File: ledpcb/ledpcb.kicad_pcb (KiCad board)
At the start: 2 copper layers, 12 parts, among them J1 USB_C_Receptacle_USB2.0, J2 Conn_01x04_Male, Q1 ME2306A, Q2 ME2306A, Q3 ME2306A, SW1 SW_Push, U1 SPX3819M5-L-3-3_TR, U2 ESP32-WROOM-32

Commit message: version
Signed-off-by: 3nt3 <gott@3nt3.de>
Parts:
- removed R4: 5.1k, Resistor_SMD:R_1206_3216Metric_Pad1.30x1.75mm_HandSolder
- added J3: Barrel_Jack, Library:DEALON DC-S050-200, F.Cu at (108.0, 109.6)
- added J4: Conn_01x04_Male, Connector_PinHeader_2.00mm:PinHeader_1x04_P2.00mm_Horizontal, F.Cu at (146.8, 100.6)
- added U3: TMP100, Package_TO_SOT_SMD:SOT-23-6, F.Cu at (106.9, 98.0)
- J1: value USB_C_Receptacle_USB2.0 -> Conn_01x02_Female; footprint Connector_USB:USB_C_Receptacle_GCT_USB4085 -> Connector_PinHeader_1.27mm:PinHeader_1x02_P1.27mm_Vertical
- J2: value Conn_01x04_Male -> Conn_01x04_Female
- R1: value 1M -> 5.1k
- R2, R3: value 5.1k -> 5K1; footprint Resistor_SMD:R_1206_3216Metric_Pad1.30x1.75mm_HandSolder -> Resistor_SMD:R_0603_1608Metric_Pad0.98x0.95mm_HandSolder
- SW1: footprint Button_Switch_SMD:SW_Push_1P1T_NO_CK_KSC6xxJ -> easyeda2kicad:KEY-SMD_4P-L6.2-W6.5-P4.50-LS8.0_SKHMXX
- moved R2 51.8 mm to (103.5, 96.8), turned to 0 degrees
- moved R1 40.3 mm to (115.1, 97.6), turned to 90 degrees
- moved J2 31.7 mm to (146.8, 86.0), turned to 0 degrees
- moved Q2 25.7 mm to (140.5, 107.6), turned to 180 degrees
- moved Q1 23.9 mm to (140.5, 101.0), turned to 180 degrees
- moved Q3 22.0 mm to (140.5, 104.3), turned to 180 degrees
- moved SW1 21.5 mm to (107.1, 88.6), turned to -90 degrees
- moved U1 15.2 mm to (142.8, 97.2), turned to -90 degrees
- moved J1 15.2 mm to (146.8, 95.8), turned to 0 degrees
- moved R3 15.0 mm to (103.4, 98.4)
- moved U2 11.5 mm to (126.7, 99.2)
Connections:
- J2 pad 1: GND -> +3V3
- J2 pad 2: Net-(J2-Pad2) -> GND
- J2 pad 3: Net-(J2-Pad3) -> TX
- J2 pad 4: Net-(J2-Pad4) -> GND
- Q1 pad 3: Net-(J2-Pad4) -> Net-(J4-Pad4)
- Q2 pad 3: Net-(J2-Pad3) -> Net-(J4-Pad3)
- Q3 pad 3: Net-(J2-Pad2) -> Net-(J4-Pad2)
- R1 pad 1: Net-(J1-PadS1) -> EN
- R1 pad 2: GND -> +3V3
- R2 pad 1: Net-(J1-PadB5) -> +3V3
- R2 pad 2: GND -> SCL
- R3 pad 1: EN -> +3V3
- R3 pad 2: +3V3 -> SDA
- U2 pad 23: RED_CHANNEL -> unconnected-(U2-Pad23)
- U2 pad 25: unconnected-(U2-Pad25) -> IO0/BOOT
- U2 pad 29: unconnected-(U2-Pad29) -> RED_CHANNEL
- U2 pad 33: unconnected-(U2-Pad33) -> SDA
- U2 pad 34: unconnected-(U2-Pad34) -> GND
- U2 pad 35: unconnected-(U2-Pad35) -> TX
- U2 pad 36: unconnected-(U2-Pad36) -> SCL
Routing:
- net +3V3: track 0.00 -> 62.8 mm, vias 0 -> 4
- net +5V: track 20.2 -> 63.7 mm
- net SCL: track 0.00 -> 41.1 mm, vias 0 -> 4
- net SDA: track 0.00 -> 35.4 mm, vias 0 -> 2
- net GND: track 0.00 -> 34.1 mm, vias 0 -> 6
- net EN: track 0.00 -> 20.0 mm
- net IO0/BOOT: track 0.00 -> 18.7 mm, vias 0 -> 2
- net Net-(J1-PadB5): track 14.7 -> 0.00 mm, vias 1 -> 0
- net TX: track 0.00 -> 13.5 mm
- net Net-(J4-Pad4): track 0.00 -> 12.2 mm, vias 0 -> 2
- net Net-(J1-PadS1): track 9.67 -> 0.00 mm
- net Net-(J4-Pad3): track 0.00 -> 6.35 mm
- net unconnected-(J1-PadA5): track 5.87 -> 0.00 mm
- net Net-(J4-Pad2): track 0.00 -> 5.79 mm
- net RED_CHANNEL: track 0.00 -> 5.12 mm
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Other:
- board outline added: 49 x 35.8 mm
- board text added: "LED Controller v1"
- board text added: "© 3nt3 2022"

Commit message: progress
Signed-off-by: 3nt3 <gott@3nt3.de>
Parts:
- added REF**: MountingHole_3.2mm_M3, MountingHole:MountingHole_3.2mm_M3, F.Cu at (106.4, 78.2)
- added REF**: MountingHole_3.2mm_M3, MountingHole:MountingHole_3.2mm_M3, F.Cu at (144.9, 122.5)
- added REF**: MountingHole_3.2mm_M3, MountingHole:MountingHole_3.2mm_M3, F.Cu at (106.2, 122.2)
- added REF**: MountingHole_3.2mm_M3, MountingHole:MountingHole_3.2mm_M3, F.Cu at (145.1, 78.2)
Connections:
- J2 pad 2: GND -> RX
- J4 pad 1: GND -> +5V
- Q1 pad 2: +5V -> GND
- Q2 pad 2: +5V -> GND
- Q3 pad 2: +5V -> GND
- U2 pad 34: GND -> RX
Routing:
- net RX: track 0.00 -> 15.1 mm, vias 0 -> 2
- net +5V: track 63.7 -> 57.7 mm, vias 0 -> 3
- net +3V3: track 62.8 -> 65.2 mm
- net GND: track 34.1 -> 32.5 mm, vias 6 -> 8
- net SDA: track 35.4 -> 34.2 mm
- net SCL: track 41.1 -> 40.3 mm
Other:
- board size 49 x 35.8 mm -> 49 x 53.3 mm
- board text added: "+5V"
- board text added: "B"
- board text added: "G"
- board text added: "R"
- board text added: "RESET"
- board text added: "Raum für Notizen"

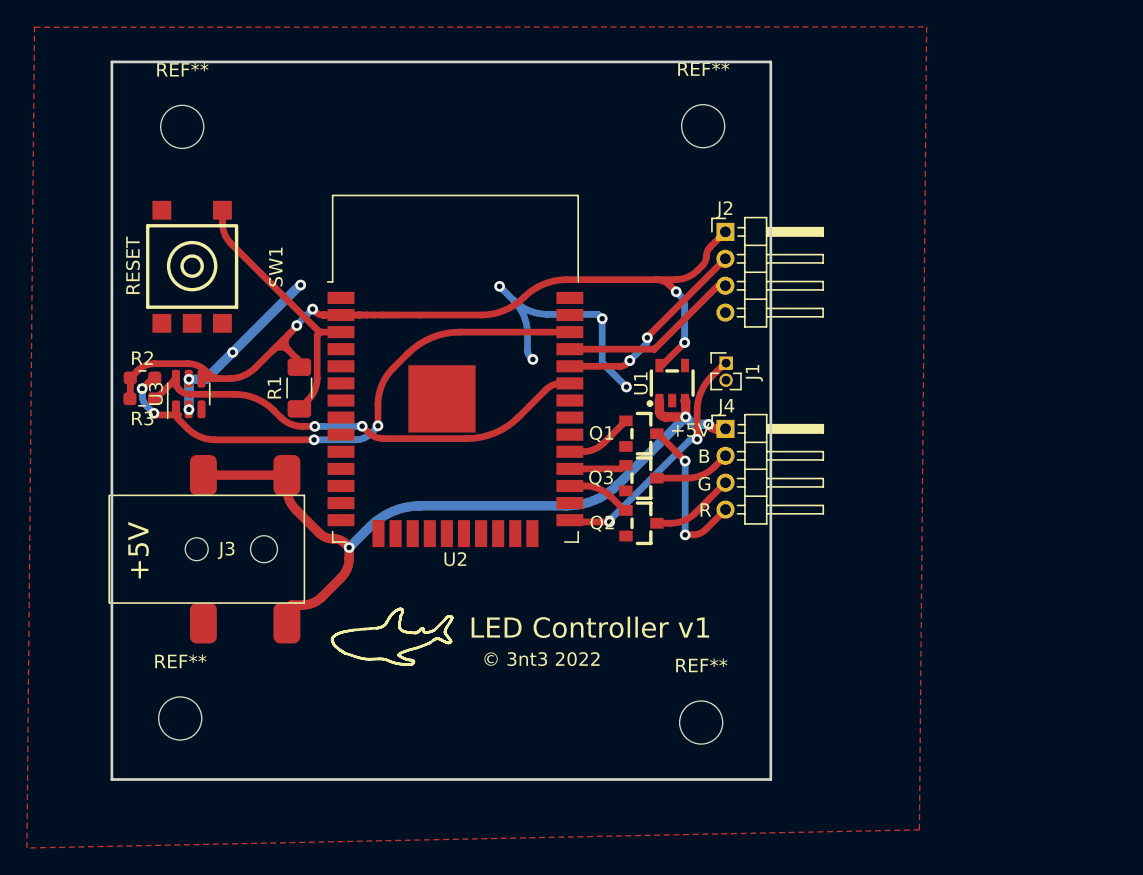
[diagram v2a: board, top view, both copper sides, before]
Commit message: add usb c receptable
Signed-off-by: 3nt3 <gott@3nt3.de>
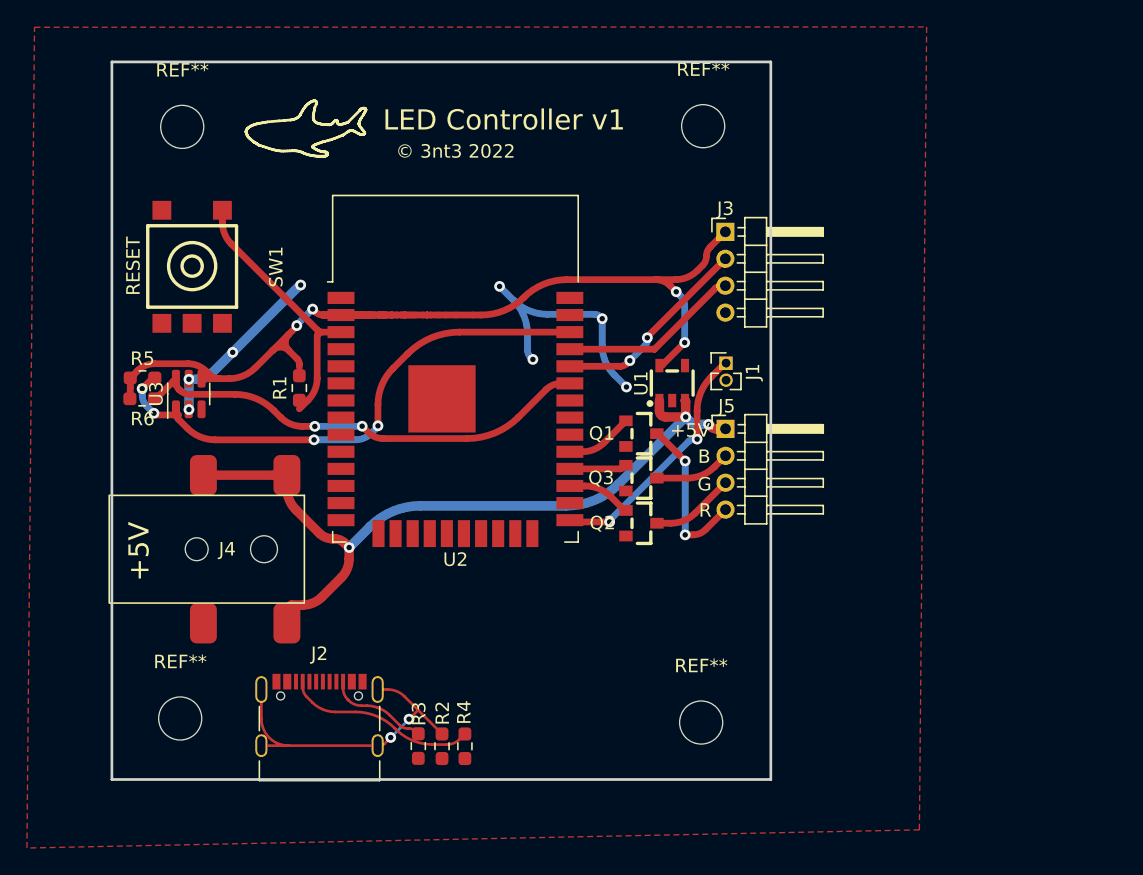
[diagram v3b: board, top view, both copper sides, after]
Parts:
- added J2: USB_C_Receptacle_USB2.0, Connector_USB:USB_C_Receptacle_Palconn_UTC16-G, F.Cu at (116.6, 121.9)
- added R2: 1M, Resistor_SMD:R_0603_1608Metric_Pad0.98x0.95mm_HandSolder, F.Cu at (125.7, 124.2)
- added R3: 5K1, Resistor_SMD:R_0603_1608Metric_Pad0.98x0.95mm_HandSolder, F.Cu at (123.9, 124.2)
- added R4: 5K1, Resistor_SMD:R_0603_1608Metric_Pad0.98x0.95mm_HandSolder, F.Cu at (127.4, 124.2)
- R1: footprint Resistor_SMD:R_1206_3216Metric_Pad1.30x1.75mm_HandSolder -> Resistor_SMD:R_0603_1608Metric_Pad0.98x0.95mm_HandSolder
- renumbered J2 to J3, J3 to J4, J4 to J5, R2 to R5, R3 to R6
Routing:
- net Net-(J2-PadS1): track 0.00 -> 24.0 mm, vias 0 -> 2
- net Net-(J2-PadA5): track 0.00 -> 14.2 mm
- net Net-(J2-PadB5): track 0.00 -> 7.46 mm

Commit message: final?
Signed-off-by: 3nt3 <gott@3nt3.de>
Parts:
- R1: value 5.1k -> 5K1
- R2: footprint Resistor_SMD:R_0603_1608Metric_Pad0.98x0.95mm_HandSolder -> Resistor_SMD:R_2512_6332Metric_Pad1.40x3.35mm_HandSolder
- moved R2 11.5 mm to (133.0, 115.3), turned to 180 degrees
- moved J2 10.8 mm to (127.4, 121.4)
- moved R3 9.63 mm to (127.7, 115.3), turned to 90 degrees
- moved R4 9.20 mm to (125.1, 115.3), turned to 90 degrees
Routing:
- net +5V: track 57.7 -> 73.8 mm
- net Net-(J2-PadA5): track 14.2 -> 3.02 mm
- net GND: track 32.2 -> 36.6 mm
- net Net-(J2-PadB5): track 7.46 -> 3.26 mm
- net Net-(J2-PadS1): track 24.0 -> 22.4 mm, vias 2 -> 0
- net EN: track 20.0 -> 19.4 mm

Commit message: whatever
Signed-off-by: 3nt3 <gott@3nt3.de>
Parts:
- J1: footprint Connector_PinHeader_1.27mm:PinHeader_1x02_P1.27mm_Vertical -> Connector_PinHeader_2.00mm:PinHeader_1x02_P2.00mm_Vertical
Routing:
- net GND: track 36.6 -> 39.3 mm
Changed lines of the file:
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@@
     (tags "mounting hole 3.2mm no annular m3")
     (attr exclude_from_pos_files exclude_from_bom)
-    (fp_text reference "REF**" (at 0 -4.2) (layer "F.SilkS")
+    (fp_text reference "REF**" (at 0 -3.0922) (layer "F.SilkS") hide
       (effects (font (size 1 1) (thickness 0.15)))
     )
@@
     (tags "mounting hole 3.2mm no annular m3")
     (attr exclude_from_pos_files exclude_from_bom)
-    (fp_text reference "REF**" (at 0 -4.2) (layer "F.SilkS")
+    (fp_text reference "REF**" (at 0.0586 -3.0192) (layer "F.SilkS") hide
       (effects (font (size 1 1) (thickness 0.15)))
     )
@@
     (fp_line (start -3.15 1.6) (end -3.15 -1.6) (layer "F.Fab") (width 0.1))
     (fp_line (start -3.15 -1.6) (end 3.15 -1.6) (layer "F.Fab") (width 0.1))
-    (pad "1" smd roundrect (at -3.05 0 180) (size 1.4 3.35) (layers "F.Cu" "F.Paste" "F.Mask") (roundrect_rratio 0.178571)
+    (pad "1" smd roundrect (at -3.05 0 180) (size 1.4 3.35) (layers "F.Cu" "F.Paste" "F.Mask") (roundrect_rratio 0.1785707143)
       (net 47 "Net-(J2-PadS1)") (pintype "passive"))
-    (pad "2" smd roundrect (at 3.05 0 180) (size 1.4 3.35) (layers "F.Cu" "F.Paste" "F.Mask") (roundrect_rratio 0.178571)
+    (pad "2" smd roundrect (at 3.05 0 180) (size 1.4 3.35) (layers "F.Cu" "F.Paste" "F.Mask") (roundrect_rratio 0.1785707143)
       (net 1 "GND") (pintype "passive"))
     (model "${KICAD6_3DMODEL_DIR}/Resistor_SMD.3dshapes/R_2512_6332Metric.wrl"
@@
     (tags "mounting hole 3.2mm no annular m3")
     (attr exclude_from_pos_files exclude_from_bom)
-    (fp_text reference "REF**" (at 0 -4.2) (layer "F.SilkS")
+    (fp_text reference "REF**" (at 0.0236 -3.0494) (layer "F.SilkS") hide
       (effects (font (size 1 1) (thickness 0.15)))
     )
@@
     )
   )
-  (footprint "Connector_PinHeader_1.27mm:PinHeader_1x02_P1.27mm_Vertical" (layer "F.Cu")
+  (footprint "Connector_PinHeader_2.00mm:PinHeader_1x02_P2.00mm_Vertical" (layer "F.Cu")
     (at 146.8 95.75)
-    (descr "Through hole straight pin header, 1x02, 1.27mm pitch, single row")
-    (tags "Through hole pin header THT 1x02 1.27mm single row")
+    (descr "Through hole straight pin header, 1x02, 2.00mm pitch, single row")
+    (tags "Through hole pin header THT 1x02 2.00mm single row")
     (property "Sheetfile" "ledpcb.kicad_sch")
     (property "Sheetname" "")
     (attr through_hole)
-    (fp_text reference "J1" (at 2 0.65 90) (layer "F.SilkS")
-      (effects (font (size 1 1) (thickness 0.15)))
-    )
-    (fp_text value "Conn_01x02_Female" (at 0 2.965) (layer "F.Fab")
-      (effects (font (size 1 1) (thickness 0.15)))
-    )
-    (fp_text user "${REFERENCE}" (at 0 0.635 90) (layer "F.Fab")
-      (effects (font (size 1 1) (thickness 0.15)))
-    )
-    (fp_line (start -1.11 0.76) (end -0.563471 0.76) (layer "F.SilkS") (width 0.12))
-    (fp_line (start -1.11 -0.76) (end 0 -0.76) (layer "F.SilkS") (width 0.12))
-    (fp_line (start -1.11 0.76) (end -1.11 1.965) (layer "F.SilkS") (width 0.12))
-    (fp_line (start 1.11 0.76) (end 1.11 1.965) (layer "F.SilkS") (width 0.12))
-    (fp_line (start -1.11 1.965) (end -0.30753 1.965) (layer "F.SilkS") (width 0.12))
-    (fp_line (start 0.563471 0.76) (end 1.11 0.76) (layer "F.SilkS") (width 0.12))
-    (fp_line (start 0.30753 1.965) (end 1.11 1.965) (layer "F.SilkS") (width 0.12))
-    (fp_line (start -1.11 0) (end -1.11 -0.76) (layer "F.SilkS") (width 0.12))
-    (fp_line (start -1.55 2.45) (end 1.55 2.45) (layer "F.CrtYd") (width 0.05))
-    (fp_line (start 1.55 -1.15) (end -1.55 -1.15) (layer "F.CrtYd") (width 0.05))
-    (fp_line (start 1.55 2.45) (end 1.55 -1.15) (layer "F.CrtYd") (width 0.05))
-    (fp_line (start -1.55 -1.15) (end -1.55 2.45) (layer "F.CrtYd") (width 0.05))
-    (fp_line (start -1.05 -0.11) (end -0.525 -0.635) (layer "F.Fab") (width 0.1))
-    (fp_line (start -0.525 -0.635) (end 1.05 -0.635) (layer "F.Fab") (width 0.1))
-    (fp_line (start 1.05 -0.635) (end 1.05 1.905) (layer "F.Fab") (width 0.1))
-    (fp_line (start -1.05 1.905) (end -1.05 -0.11) (layer "F.Fab") (width 0.1))
-    (fp_line (start 1.05 1.905) (end -1.05 1.905) (layer "F.Fab") (width 0.1))
-    (pad "1" thru_hole rect (at 0 0) (size 1 1) (drill 0.65) (layers *.Cu *.Mask)
+    (fp_text reference "J1" (at 0 -2.06) (layer "F.SilkS")
+      (effects (font (size 1 1) (thickness 0.15)))
+    )
+    (fp_text value "Conn_01x02_Female" (at 0 4.06) (layer "F.Fab")
+      (effects (font (size 1 1) (thickness 0.15)))
+    )
+    (fp_text user "${REFERENCE}" (at 0 1 90) (layer "F.Fab")
+      (effects (font (size 1 1) (thickness 0.15)))
+    )
+    (fp_line (start -1.06 1) (end -1.06 3.06) (layer "F.SilkS") (width 0.12))
+    (fp_line (start -1.06 1) (end 1.06 1) (layer "F.SilkS") (width 0.12))
+    (fp_line (start -1.06 3.06) (end 1.06 3.06) (layer "F.SilkS") (width 0.12))
+    (fp_line (start -1.06 -1.06) (end 0 -1.06) (layer "F.SilkS") (width 0.12))
+    (fp_line (start 1.06 1) (end 1.06 3.06) (layer "F.SilkS") (width 0.12))
+    (fp_line (start -1.06 0) (end -1.06 -1.06) (layer "F.SilkS") (width 0.12))
+    (fp_line (start -1.5 -1.5) (end -1.5 3.5) (layer "F.CrtYd") (width 0.05))
+    (fp_line (start -1.5 3.5) (end 1.5 3.5) (layer "F.CrtYd") (width 0.05))
+    (fp_line (start 1.5 -1.5) (end -1.5 -1.5) (layer "F.CrtYd") (width 0.05))
+    (fp_line (start 1.5 3.5) (end 1.5 -1.5) (layer "F.CrtYd") (width 0.05))
+    (fp_line (start 1 -1) (end 1 3) (layer "F.Fab") (width 0.1))
+    (fp_line (start 1 3) (end -1 3) (layer "F.Fab") (width 0.1))
+    (fp_line (start -1 3) (end -1 -0.5) (layer "F.Fab") (width 0.1))
+    (fp_line (start -0.5 -1) (end 1 -1) (layer "F.Fab") (width 0.1))
+    (fp_line (start -1 -0.5) (end -0.5 -1) (layer "F.Fab") (width 0.1))
+    (pad "1" thru_hole rect (at 0 0) (size 1.35 1.35) (drill 0.8) (layers *.Cu *.Mask)
       (net 25 "IO0{slash}BOOT") (pinfunction "Pin_1") (pintype "passive"))
-    (pad "2" thru_hole oval (at 0 1.27) (size 1 1) (drill 0.65) (layers *.Cu *.Mask)
+    (pad "2" thru_hole oval (at 0 2) (size 1.35 1.35) (drill 0.8) (layers *.Cu *.Mask)
       (net 1 "GND") (pinfunction "Pin_2") (pintype "passive"))
-    (model "${KICAD6_3DMODEL_DIR}/Connector_PinHeader_1.27mm.3dshapes/PinHeader_1x02_P1.27mm_Vertical.wrl"
+    (model "${KICAD6_3DMODEL_DIR}/Connector_PinHeader_2.00mm.3dshapes/PinHeader_1x02_P2.00mm_Vertical.wrl"
       (offset (xyz 0 0 0))
       (scale (xyz 1 1 1))
@@
     (tags "mounting hole 3.2mm no annular m3")
     (attr exclude_from_pos_files exclude_from_bom)
-    (fp_text reference "REF**" (at 0 -4.2) (layer "F.SilkS")
+    (fp_text reference "REF**" (at 0.061 -2.6612) (layer "F.SilkS") hide
       (effects (font (size 1 1) (thickness 0.15)))
     )
@@
     (effects (font (size 1 1) (thickness 0.15)))
   )
+  (segment (start 130.3528 117.6274) (end 130.0226 117.6274) (width 0.2) (layer "F.Cu") (net 1))
   (segment (start 130.2856 115.6064) (end 129.9952 115.316) (width 0.2) (layer "F.Cu") (net 1))
+  (segment (start 130.576 118.9005) (end 130.576 118.1154) (width 0.2) (layer "F.Cu") (net 1))
+  (segment (start 130.576 118.1154) (end 130.6068 118.0846) (width 0.2) (layer "F.Cu") (net 1))
   (segment (start 108.5175 115.075) (end 107.975 115.075) (width 0.2) (layer "F.Cu") (net 1))
-  (segment (start 130.576 116.307487) (end 130.576 118.9005) (width 0.2) (layer "F.Cu") (net 1))
+  (segment (start 129.9952 117.6) (end 129.9952 115.316) (width 0.2) (layer "F.Cu") (net 1))
+  (segment (start 124.176 118.9005) (end 124.176 118.6896) (width 0.2) (layer "F.Cu") (net 1))
+  (segment (start 130.6068 118.0846) (end 130.6068 117.8814) (width 0.2) (layer "F.Cu") (net 1))
+  (segment (start 124.176 118.6896) (end 123.4186 117.9322) (width 0.2) (layer "F.Cu") (net 1))
+  (segment (start 130.0226 117.6274) (end 129.9952 117.6) (width 0.2) (layer "F.Cu") (net 1))
+  (segment (start 130.6068 117.8814) (end 130.3528 117.6274) (width 0.2) (layer "F.Cu") (net 1))
   (via (at 106.9 99.2) (size 0.8) (drill 0.4) (layers "F.Cu" "B.Cu") (net 1))
   (via (at 106.9 96.95) (size 0.8) (drill 0.4) (layers "F.Cu" "B.Cu") (net 1))
